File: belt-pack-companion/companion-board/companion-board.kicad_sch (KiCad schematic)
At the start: 38 parts, among them J1 Conn_01x18_Socket, J2 Conn_01x18_Socket, J3 AudioJack4_Ground, J4 Micro_SD_Card, U1 TLV320AIC3204

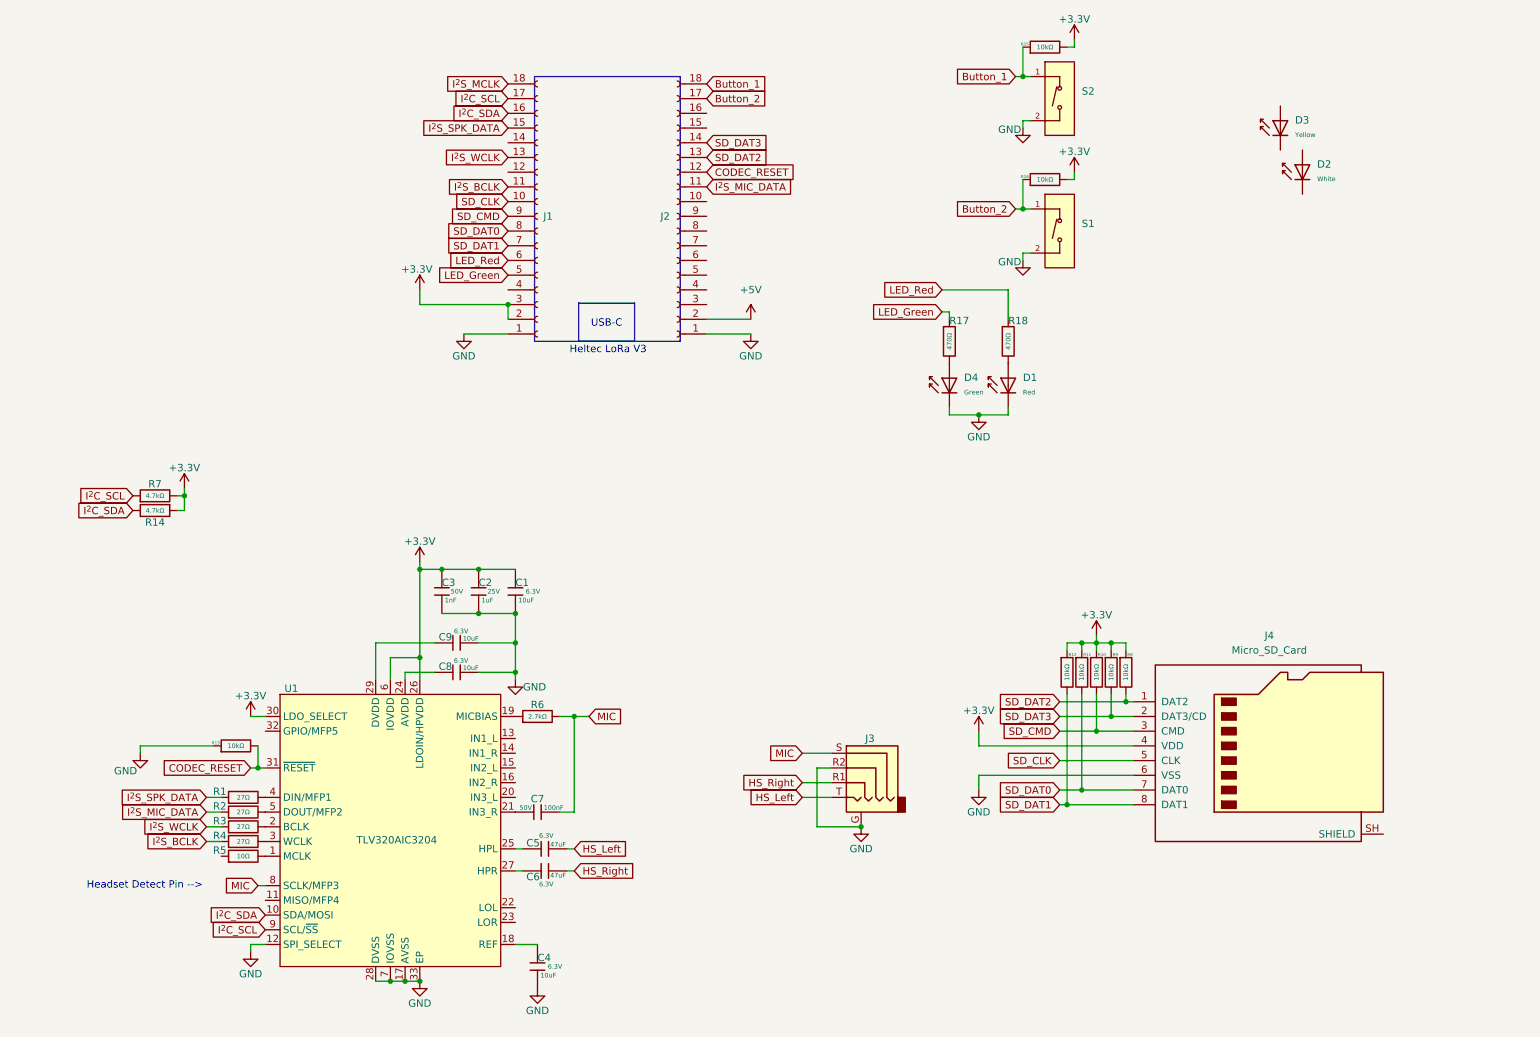
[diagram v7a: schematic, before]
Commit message: Schematic Updates
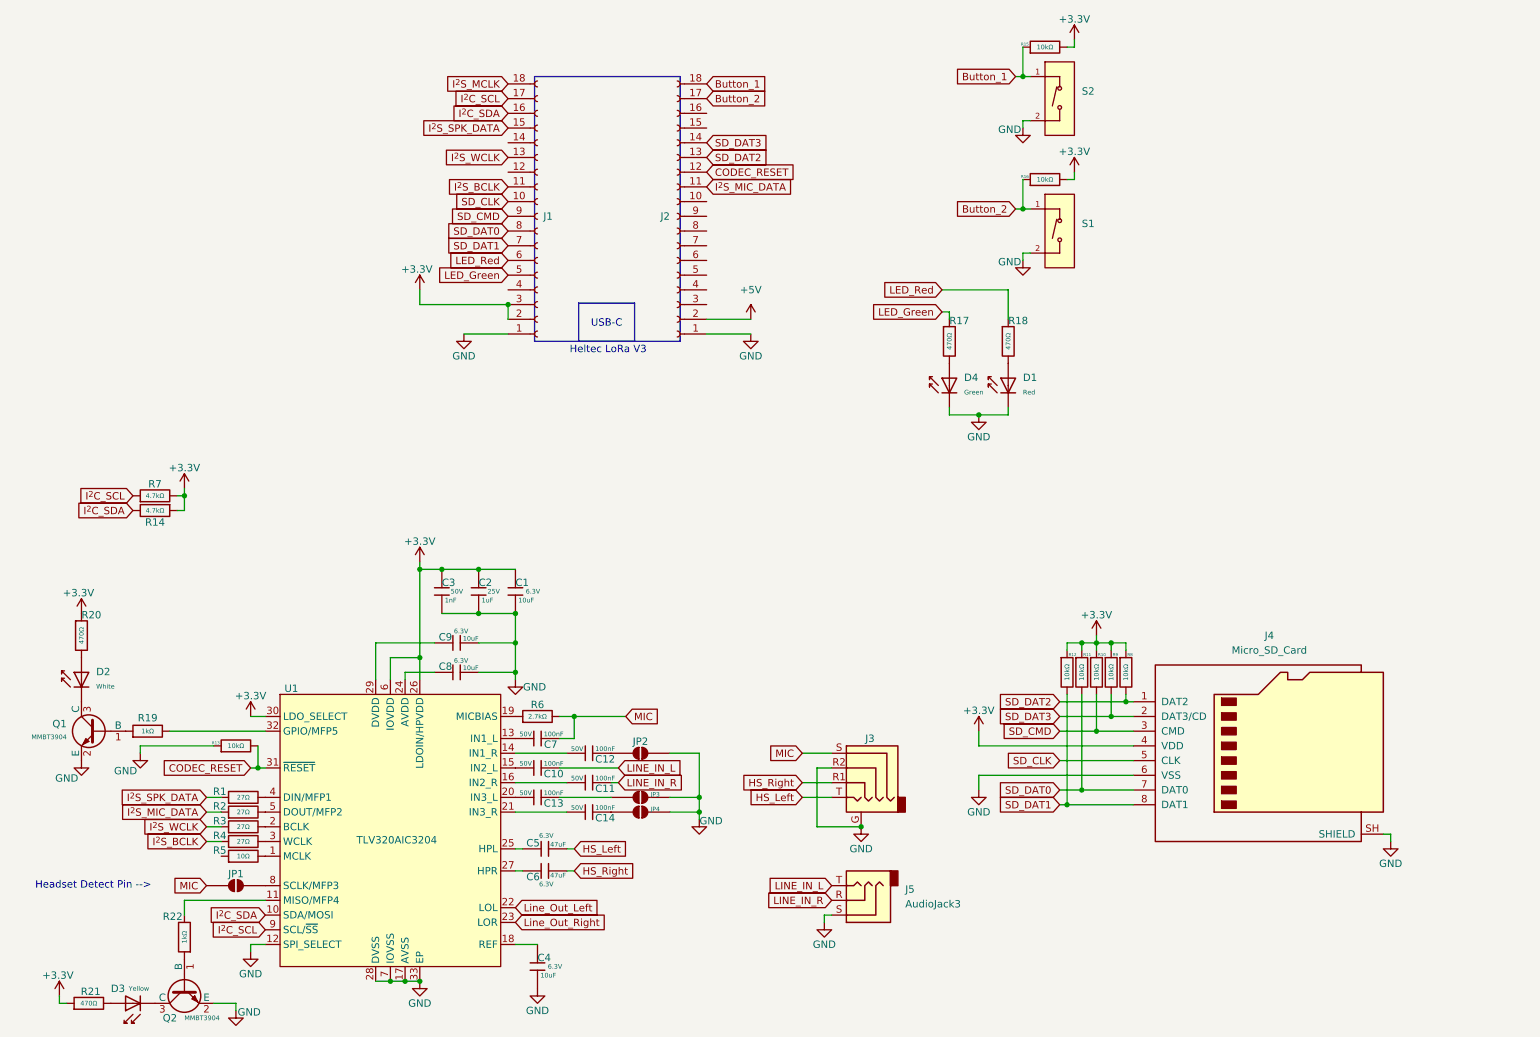
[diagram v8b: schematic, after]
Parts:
- added C10, C11, C12, C13, C14: 100nF, PCM_JLCPCB:C_0603, symbol PCM_JLCPCB-Capacitors:0603,100nF
- added J5: AudioJack3, symbol Connector_Audio:AudioJack3
- added JP1, JP2, JP3, JP4: SolderJumper_2_Open, symbol Jumper:SolderJumper_2_Open
- added Q1, Q2: MMBT3904, PCM_JLCPCB:Q_SOT-23, symbol PCM_JLCPCB-Transistors:NPN,MMBT3904
- added R19, R22: 1kΩ, PCM_JLCPCB:R_0402, symbol PCM_JLCPCB-Resistors:0402,1kΩ
- added R20, R21: 470Ω, PCM_JLCPCB:R_0402, symbol PCM_JLCPCB-Resistors:0402,470Ω
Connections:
- net +3.3V: now also R20.1, R21.1
- net GND: now also J4.SH (SHIELD), J5.S, JP2.2 (B), JP3.2 (B), JP4.2 (B), Q1.2 (E), Q2.2 (E)
- net MIC: now also JP1.1 (A); no longer U1.8 (SCLK/MFP3)
- net at D3.1: now also Q2.3 (C)
- net at D3.2: now also R21.2
- net at U1.11 (MISO/MFP4): now also R22.2
- net at U1.13 (IN1_L): now also C7.1
- net at U1.14 (IN1_R): now also C12.1
- net at U1.15 (IN2_L): now also C10.1
- net at U1.16 (IN2_R): now also C11.1
- net at U1.20 (IN3_L): now also C13.1
- net at U1.21 (IN3_R): now also C14.1; no longer C7.1
- net Line_Out_Left: now reaches U1.22 (LOL)
- net Line_Out_Right: now reaches U1.23 (LOR)
- net at U1.32 (GPIO/MFP5): now also R19.2
- net at D2.1: now also Q1.3 (C)
- net at D2.2: now also R20.2
- new net: Q1.1 (B), R19.1
- new net: Q2.1 (B), R22.1
- new net: C14.2, JP4.1 (A)
- new net: JP1.2 (B), U1.8 (SCLK/MFP3)
- new net: C12.2, JP2.1 (A)
- new net: C13.2, JP3.1 (A)
- new net LINE_IN_L: C10.2, J5.T
- new net LINE_IN_R: C11.2, J5.R
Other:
- moved on the sheet: D2, D3
